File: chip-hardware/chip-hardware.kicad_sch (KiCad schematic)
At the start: 9 parts

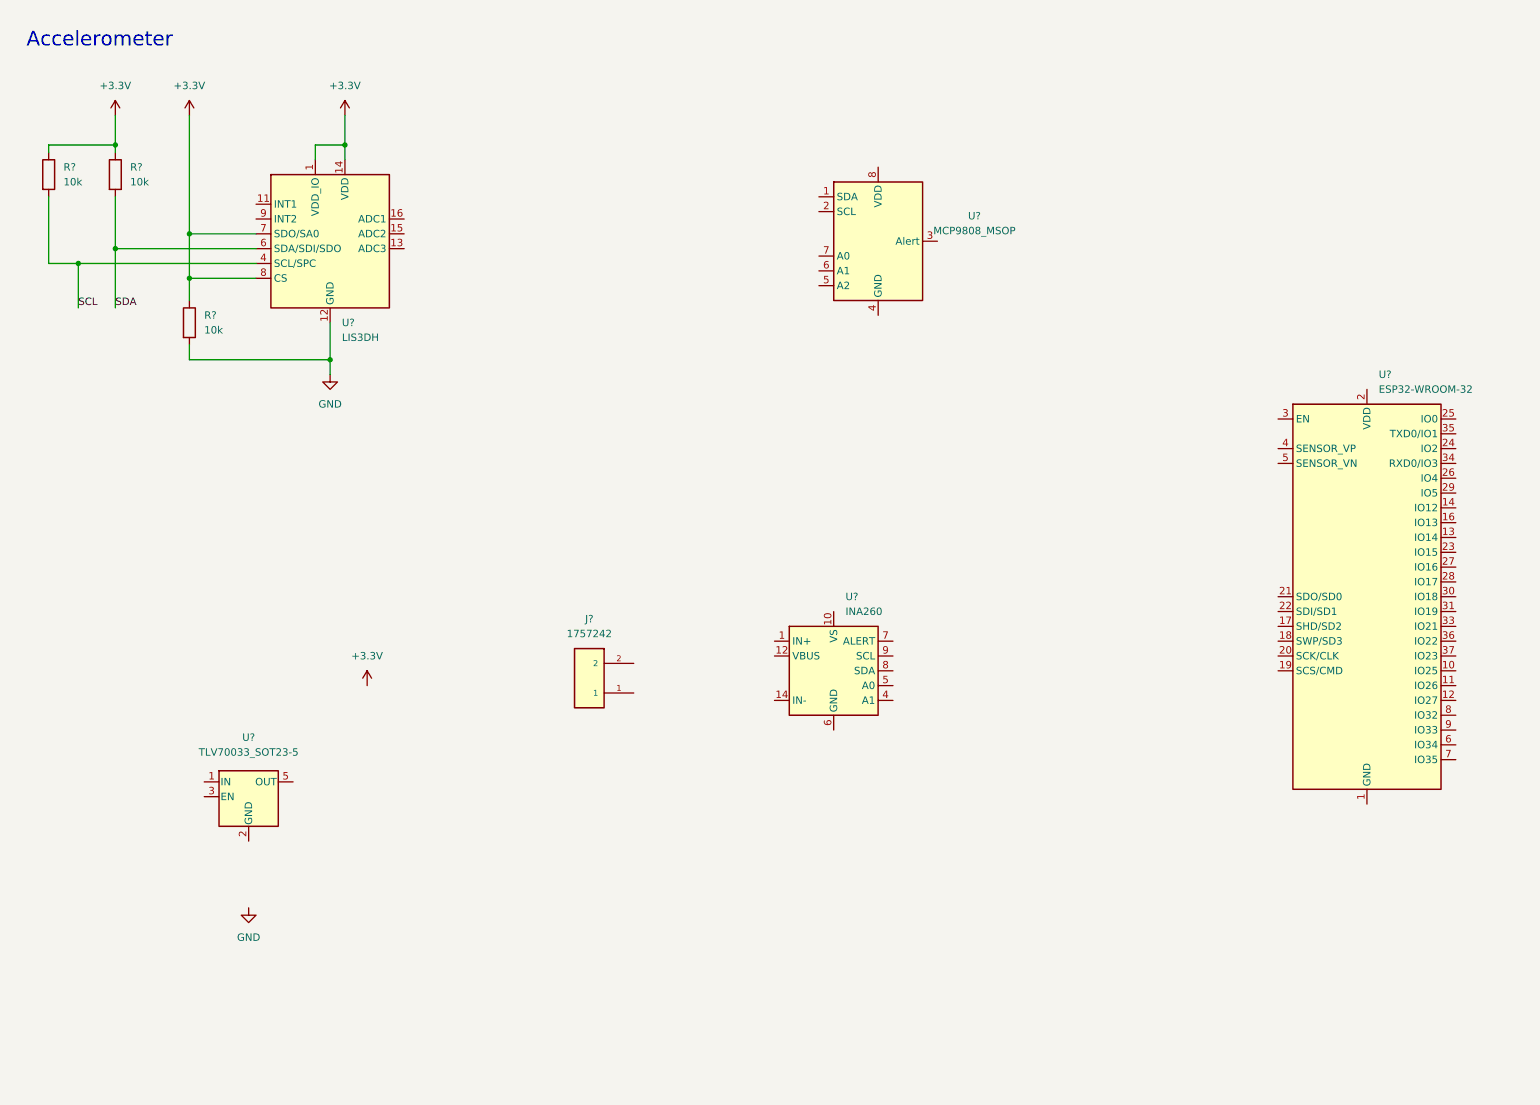
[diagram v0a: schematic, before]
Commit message: Got temperature sensor working
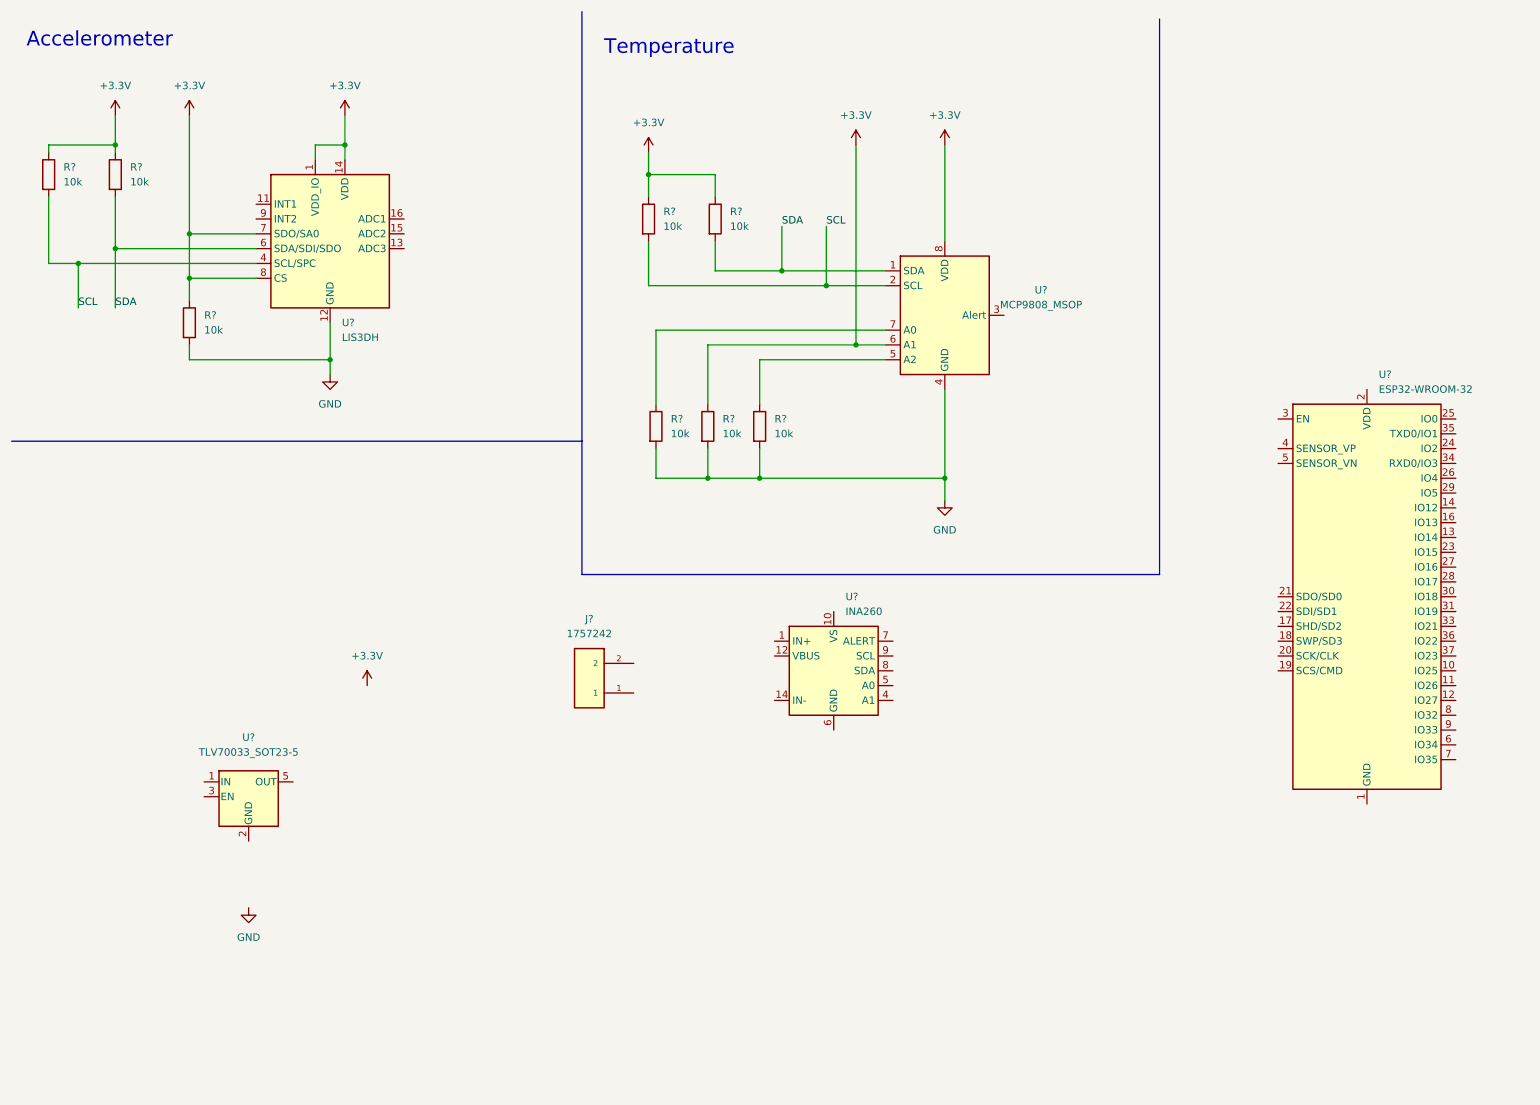
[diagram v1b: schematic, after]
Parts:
- added R? (x5): 10k, symbol Device:R
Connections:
- net +3V3: now also U?.6 (A1), U?.8 (VDD), R?.1, R?.1, R?.1
- net GND: now also U?.4 (GND), R?.2, R?.2, R?.2
- net SCL: now also U?.2 (SCL), R?.2
- net SDA: now also U?.1 (SDA), R?.2
- net at U?.5 (A2): now also R?.1
- net at U?.7 (A0): now also R?.1
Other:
- note added: "Temperature"
- moved on the sheet: U?

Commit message: Got temperature sensor working
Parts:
- added R? (x4): 10k, symbol Device:R
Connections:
- net +3V3: now also U?.10 (VS), R?.1, R?.1
- net GND: now also U?.11 (GND), U?.6 (GND), R?.2, R?.2
- net SCL: now also U?.9 (SCL), R?.2
- net SDA: now also U?.8 (SDA), R?.2
- net at J?.1: now also U?.14 (IN-), U?.15 (IN-), U?.16 (IN-)
- net at J?.2: now also U?.1 (IN+), U?.12 (VBUS), U?.2 (IN+), U?.3 (IN+)
- net at U?.4 (A1): now also R?.1
- net at U?.5 (A0): now also R?.1
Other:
- note added: "Accelerometer Sensor"
- note added: "Current Sensor"
- note added: "Microprocessor"
- note added: "Temperature Sensor"
- note added: "Voltage Regulator"
- note removed: "Accelerometer"
- note removed: "Temperature"
- moved on the sheet: J?, U?

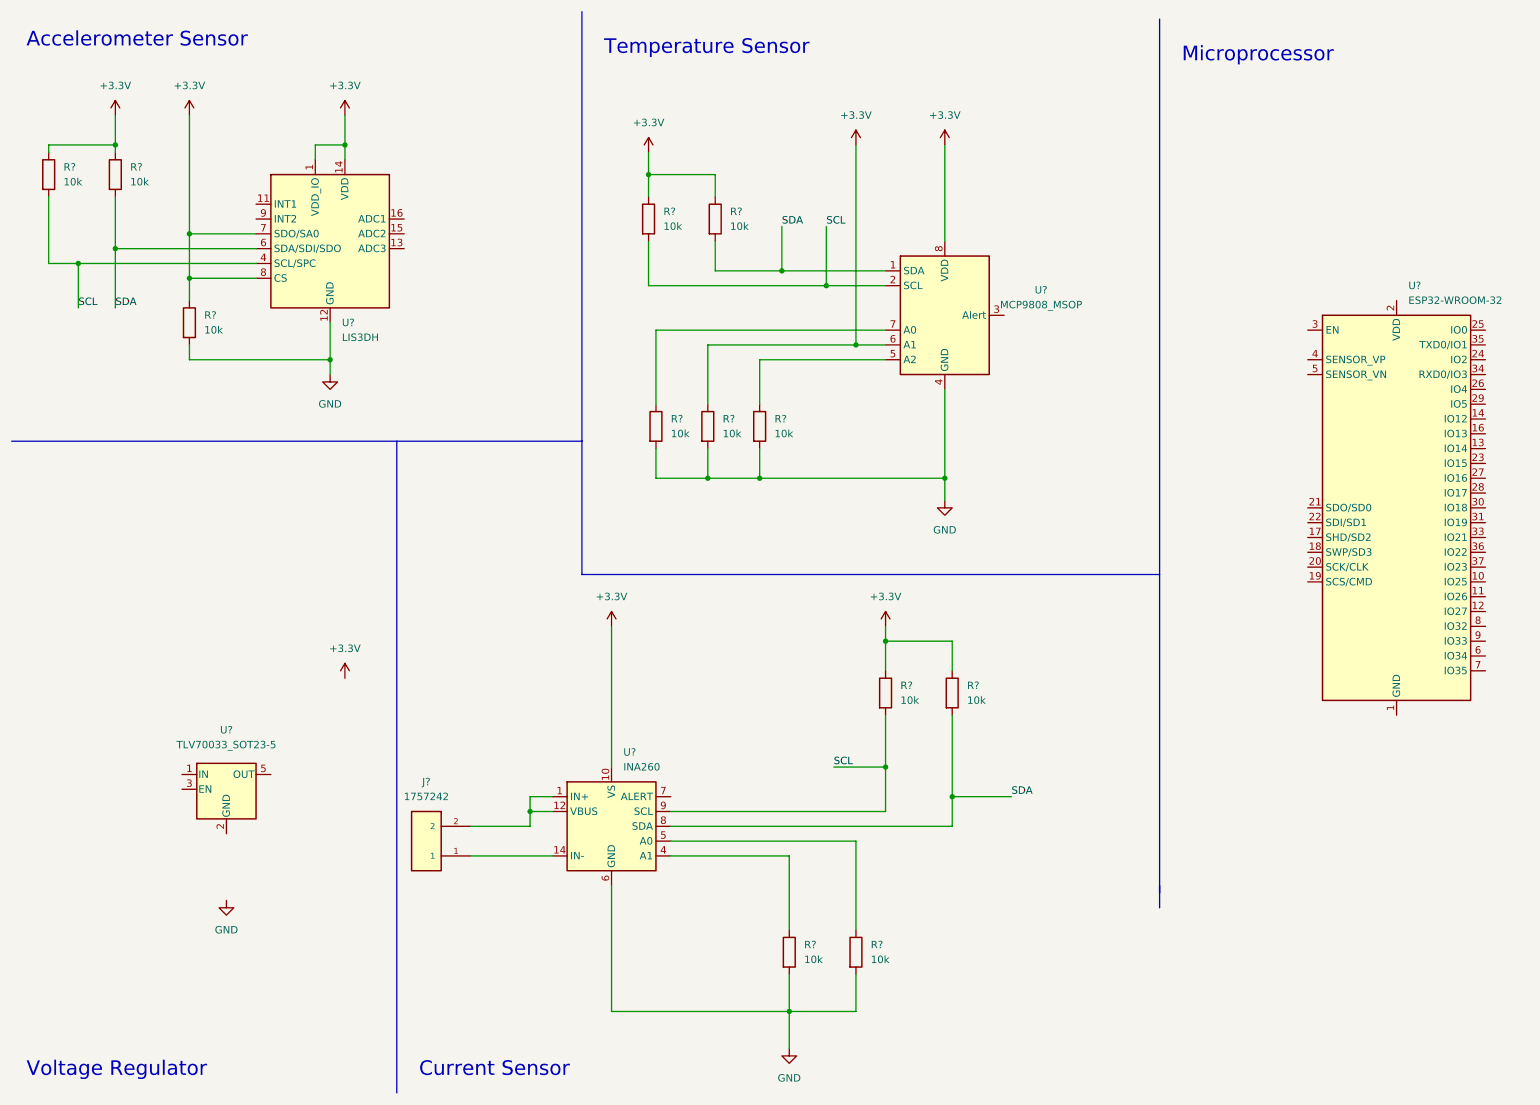
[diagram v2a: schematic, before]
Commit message: Did almost all of the microprocessor, need to finish regulator
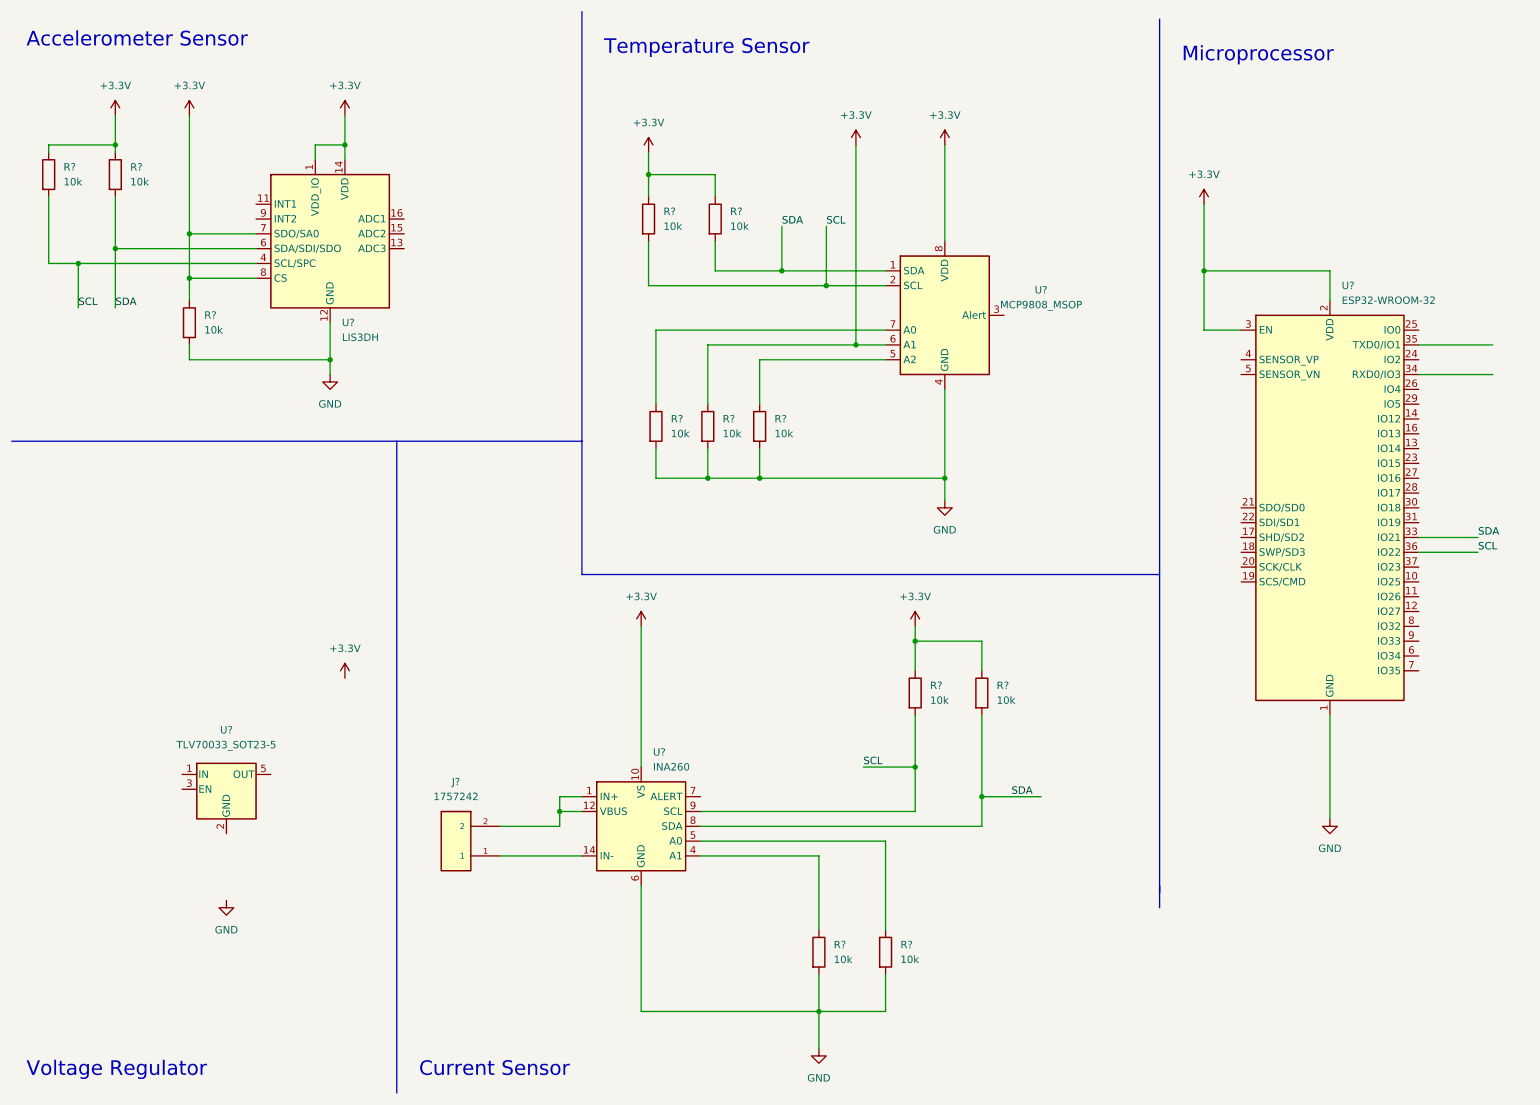
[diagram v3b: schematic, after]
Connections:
- net +3V3: now also U?.2 (VDD), U?.3 (EN)
- net GND: now also U?.1 (GND), U?.15 (GND), U?.38 (GND), U?.39 (GND)
- net SCL: now also U?.36 (IO22)
- net SDA: now also U?.33 (IO21)
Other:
- moved on the sheet: J?, R?, U?
